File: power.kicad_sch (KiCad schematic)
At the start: 44 parts, among them J2 B3B-XH-A, U5 EG11752, U6 BQ25606RGER, U9 ME6211C33M5G

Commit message: M3: F-9 review package, firmware notes, R80 pulse analysis, rules 1-9 audit, M4 prep
- docs/f9-review.md: all 76 NEEDS-HUMAN pins, 3-source verdicts (62 AGREE /
  14 CONFLICT flagged), GND + RESERVED rows first, nothing connected.
- docs/firmware-notes.md: FW-1..FW-17 + BV-1..BV-4.
- R80: selected FRP2512J100 C3013385 (2W); pulse duty computed at 8.5 mJ /
  384 W pk / tau 44 us per full-rated SMDJ strike (energy R-independent).
  F-15 NEW: 10R has NO load-line solution at the 10.5 V floor at full load -
  brown-out; recommend 1R FRS2512F1R00TS C55348540 (anti-surge). Decision gate.
- Rules audit: 1 NOT MET (F-13 X5R/6.3V modem bulk caps), 8 NOT MET (F-14
  six missing TPs: VIN, VBAT_MODEM, CANH/CANL, modem UART), rest MET/N-A
  with evidence; section-6 blocks all MET as amended.
- M4 prep: stackup defined (L1 sig/RF, L2 solid GND, L3 power, L4 sig,
  JLC7628 1.6mm); docs/placement-study.svg on PROVISIONAL 80x60 outline.
- Footprint checks: J1 posts RESOLVED (derived footprint with 2x NPTH from
  XUNPU drawing, J1 re-pointed); SIM pad map VERIFIED but posts missing ->
  F-16 (y-datum ambiguous, no copper guessed); SMF05C pin2=GND VERIFIED
  (onsemi pin table) - caveat closed; X2 remapped to authoritative ETSI/
  1GLOBAL MFF2 pinout (old 6-pin placeholder was wrong), land pattern gated
  F-17 on vendor packaging spec.

ERC 0 errors / 14 justified warnings; checkpins 48/48 + F-10 8/8 PASS.

Co-Authored-By: Claude Fable 5 <noreply@anthropic.com>
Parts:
- R80: LCSC TBD-F5-pulse -> C3013385
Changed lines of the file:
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@@
 			)
 		)
-		(property "LCSC" "TBD-F5-pulse"
+		(property "LCSC" "C3013385"
 			(at 149.86 50.8 0)
 			(hide yes)

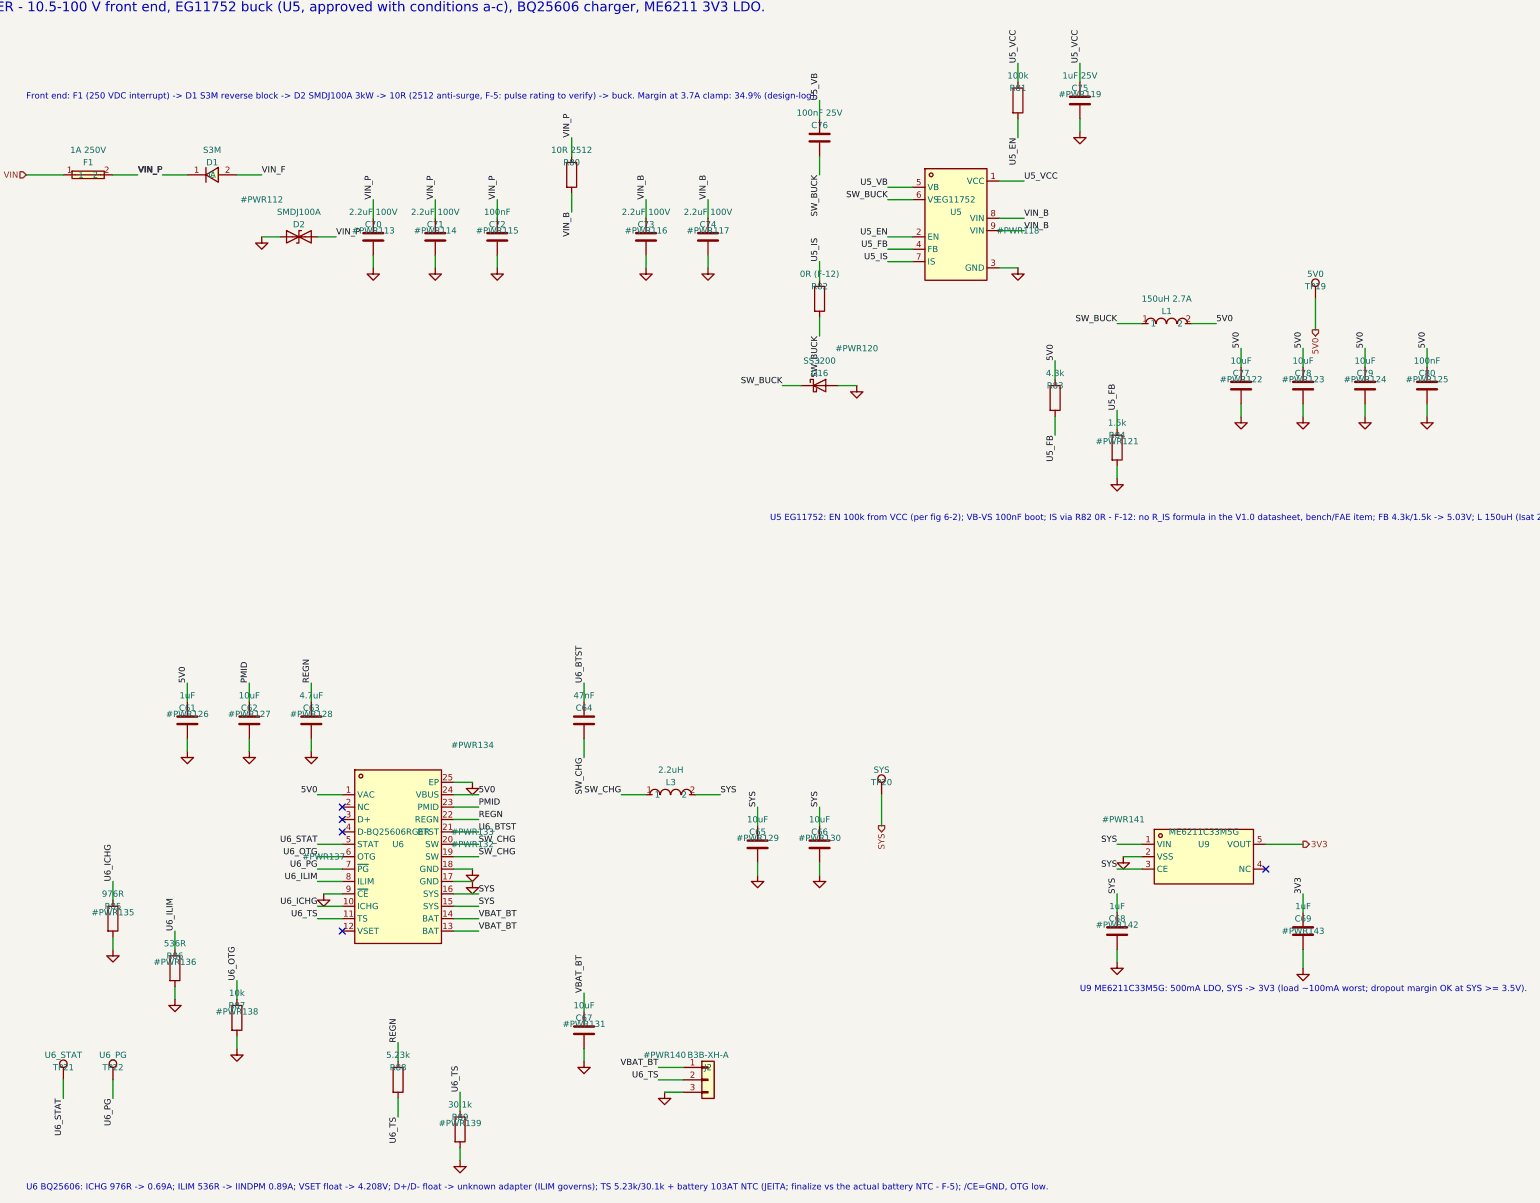
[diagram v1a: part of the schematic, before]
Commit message: M3 close: F-9 signed off - 43 GND pads connected, verified against Table 7
F-9b reverse check found the "central LGA grid = ground field" premise in
docs/f9-review.md is false: 40 of the 64 inner-field/ANT-fence pads carry
definite non-ground functions (24 already VERIFIED against Table 7). That
premise supplied the second source for pins 76 and 85-112, so the 35-pin GND
list was in fact single-source (symbol only) with Table 7 unparsed for every
row.

Resolved by reading the primary source rather than stopping on a doc defect.
Quectel EC200U Series Hardware Design V1.2 (2023-05-19), Table 7 p.21 and
Table 9 p.36 both read verbatim:

    GND    8, 9, 19, 22, 36, 46, 48, 50-54, 56, 72, 76, 85-112

= 43 GND pads; 8 already connected, so exactly the 35 on the list, pin for
pin, nothing missing or extra. F-9b verdict: CLEAN, no ground pad omitted.
Root cause of all five "unparsed" rows: the ranges use U+2013 EN DASH, not
"~" as previously recorded. Datasheet vendored into docs/ (MD5
995ce77179cf0613277111e73c640455) so the sign-off record is self-contained.

Applied via the pin-map source of truth, not by editing the schematic:
35 rows NEEDS-HUMAN -> VERIFIED, tally 68/76 -> 103/41. Conflict rows
81/82/117 (RESERVED, "keep open"; symbol uses QuecOpen names), 118
(WLAN_SLP_CLK), 128 (USIM2_VDD) and 140 (ISINK) annotated with their V1.2
readings but left NEEDS-HUMAN so they stay NC and marked. The 14 CONFLICT
pins remain NC with F9-REVIEW markers.

Thermal relief plan recorded for layout: 85-112 each stitched solid to L2 with
its own via (no spokes), RF fence 46/48/50/51 >=2 vias each, 76 and perimeter
grounds >=1 via.

Verification: modem_rf 103 -> 138 symbols (+35). ERC 0 errors / 14 warnings
unchanged. checkpins exit 0. U1 pads on GND = 44 (43 + pin 10 USIM_GND).
Net-set comparison proves the only electrical change is 35
unconnected-(U1-GND-PadNN) nets collapsing into GND: 0 nets added, exactly one
surviving net changed. power.kicad_sch diff is #PWR112->#PWR147 renumbe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
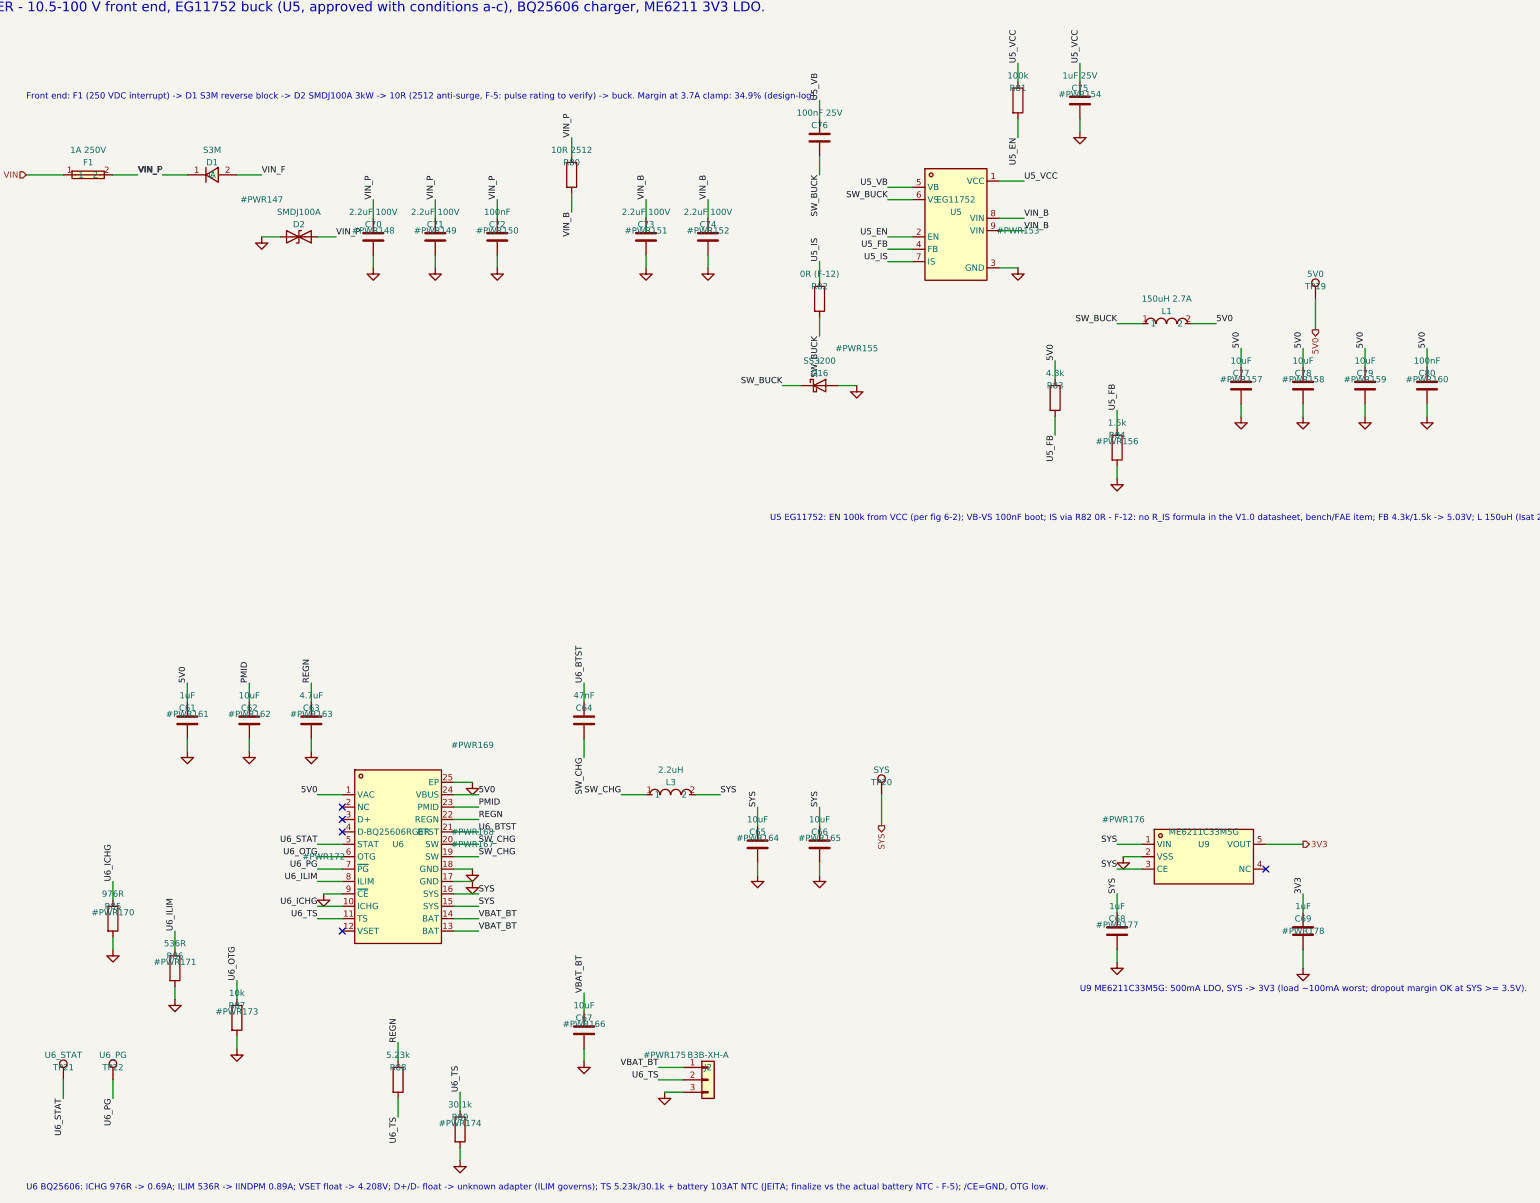
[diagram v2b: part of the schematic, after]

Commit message: M3 close: F-15 R80 1R, F-14 six test points, ambient rating, CPWG geometry
F-15: R80 10R (C3013385) -> 1R anti-surge FRS2512F1R00TS (C55348540).
At the 10.5 V floor and full load the 10R version had NO load-line solution:
V_B^2 - 9.8*V_B + 59 = 0, discriminant -140. Max power transfer through 10R
from 9.8 V is V^2/4R = 2.4 W against a 5.9 W demand - a hard brown-out. At 1R:
V_B = 9.16 V, I = 0.644 A, 0.41 W worst-case continuous, 24 W ceiling.
Pulse energy unchanged at 8.5 mJ (E = CdV^2/2 is independent of R) but peak
goes 384 W -> 3.8 kW and tau 44 us -> 4.4 us, which is why the part must be
anti-surge rather than plain thick film. Confirming that pulse curve joins F-12
on the bench list.

F-14: TP23 VIN, TP24 VBAT_MODEM, TP25 CANH, TP26 CANL, TP27 MODEM_TX,
TP28 MODEM_RX. Each verified against the netlist to share its net with the
real circuit nodes. hier() used for hierarchical nets and net() only for
sheet-local ones, so ERC stayed at exactly 0 errors / 14 warnings with no new
same_local_global_label entries. Rule 8 now MET (28 test points).

Product spec: rated operating ambient -20 to +70 C, housing shaded or
light-coloured, 85 C survival not operating - added to handoff section 1.1 and
a new docs/installation-sheet.md. Governed by U1: EC200U V1.2 Table 42 p.75
gives operating -35..+75 C (meets 3GPP) and extended -40..+85 C (functions
maintained but Pout may exceed 3GPP tolerances), so +70 C keeps 5 C to the
compliant limit and 85 C is exactly the extended limit.

NEW FLAG F-19: typical 1S Li-ion is -20..+60 C discharge, narrower than the
+70 C product ceiling. Charging is already protected by the BQ25606 JEITA
network; discharge above 60 C and calendar ageing are not. Decision needed -
accept with a shorter battery service interval, or narrow the rating to +60 C.

M4 input: 50 ohm CPWG for JLC7628 L1-L2 computed via Ghione-Naldi conformal
mapping (elliptic integrals by AGM), cross-checked against Hammerstad-Jensen
microstrip. h = 0.2104 mm (1x 7628 prepreg). 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
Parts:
- added TP23: VIN, TestPoint:TestPoint_Pad_D1.5mm, symbol Connector:TestPoint
- R80: value 10R 2512 -> 1R 2512 anti-surge; LCSC C3013385 -> C55348540
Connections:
- net VIN: now also TP23.1
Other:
- note added: "F-14 test point: VIN (HV ZONE, up to 100 V - 1.5 mm clearance)."
- note added: "Front end: F1 (250 VDC interrupt) -> D1 S3M reverse block -> D2 SMDJ100A 3kW -> R80 1R 2512 anti-surge (F-15 approved) -> buck. Margin at 3.7A clamp: 34.9%. R80 at the 10.5V floor, full load: V_B=9.16V, I=0.644A, 0.41W. 10R was a brown-out (no load-line solution) - see design-log F-15."
- note removed: "Front end: F1 (250 VDC interrupt) -> D1 S3M reverse block -> D2 SMDJ100A 3kW -> 10R (2512 anti-surge, F-5: pulse rating to verify) -> buck. Margin at 3.7A clamp: 34.9% (design-log)."
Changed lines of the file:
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@@
 		)
 	)
-	(text "Front end: F1 (250 VDC interrupt) -> D1 S3M reverse block -> D2 SMDJ100A 3kW -> 10R (2512 anti-surge, F-5: pulse rating to verify) -> buck. Margin at 3.7A clamp: 34.9% (design-log)."
+	(text "Front end: F1 (250 VDC interrupt) -> D1 S3M reverse block -> D2 SMDJ100A 3kW -> R80 1R 2512 anti-surge (F-15 approved) -> buck. Margin at 3.7A clamp: 34.9%. R80 at the 10.5V floor, full load: V_B=9.16V, I=0.644A, 0.41W. 10R was a brown-out (no load-line solution) - see design-log F-15."
 		(exclude_from_sim no)
 		(at 38.1 35.56 0)
+		(effects
+			(font
+				(size 1.27 1.27)
+			)
+			(justify left bottom)
+		)
+	)
+	(wire
+		(pts
+			(xy 30.48 271.78) (xy 30.48 276.86)
+		)
+		(stroke
+			(width 0)
+			(type default)
+		)
+	)
+	(hierarchical_label "VIN"
+		(shape input)
+		(at 30.48 276.86 270)
+		(effects
+			(font
+				(size 1.27 1.27)
+			)
+			(justify right)
+		)
+	)
+	(text "F-14 test point: VIN (HV ZONE, up to 100 V - 1.5 mm clearance)."
+		(exclude_from_sim no)
+		(at 30.48 264.16 0)
 		(effects
 			(font
@@
 			)
 		)
-		(property "Value" "10R 2512"
+		(property "Value" "1R 2512 anti-surge"
 			(at 149.86 45.72 0)
 			(effects
@@
 			)
 		)
-		(property "LCSC" "C3013385"
+		(property "LCSC" "C55348540"
 			(at 149.86 50.8 0)
 			(hide yes)
@@
 					(unit 1)
 				)
+			)
+		)
+	)
+	(symbol
+		(lib_id "Connector:TestPoint")
+		(at 30.48 271.78 0)
+		(unit 1)
+		(exclude_from_sim no)
+		(in_bom yes)
+		(on_board yes)
+		(dnp no)
+		(fields_autoplaced yes)
+		(property "Reference" "TP23"
+			(at 30.48 269.24 0)
+			(effects
+				(font
+					(size 1.27 1.27)
+				)
+			)
+		)
+		(property "Value" "VIN"
+			(at 30.48 266.7 0)
+			(effects
+				(font
+					(size 1.27 1.27)
+				)
+			)
+		)
+		(property "Footprint" "TestPoint:TestPoint_Pad_D1.5mm"
+			(at 30.48 271.78 0)
+			(hide yes)
+			(effects
+				(font
+					(size 1.27 1.27)
+				)
+			)
+		)
+		(property "Datasheet" "~"
+			(at 30.48 271.78 0)
+			(hide yes)
+			(effects
+				(font
+					(size 1.27 1.27)
+				)
+			)
+		)
+		(pin "1"
+		)
+		(instances
+			(project "telematics-tracker"
+				(path "/784bc421-9fc7-43cb-bfc3-562714cb3f68/9e25249c-17f3-52b0-bdea-48010d482c2d"
+					(reference "TP23")
+					(unit 1)
+				)
